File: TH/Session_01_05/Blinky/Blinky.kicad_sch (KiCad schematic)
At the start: 8 parts

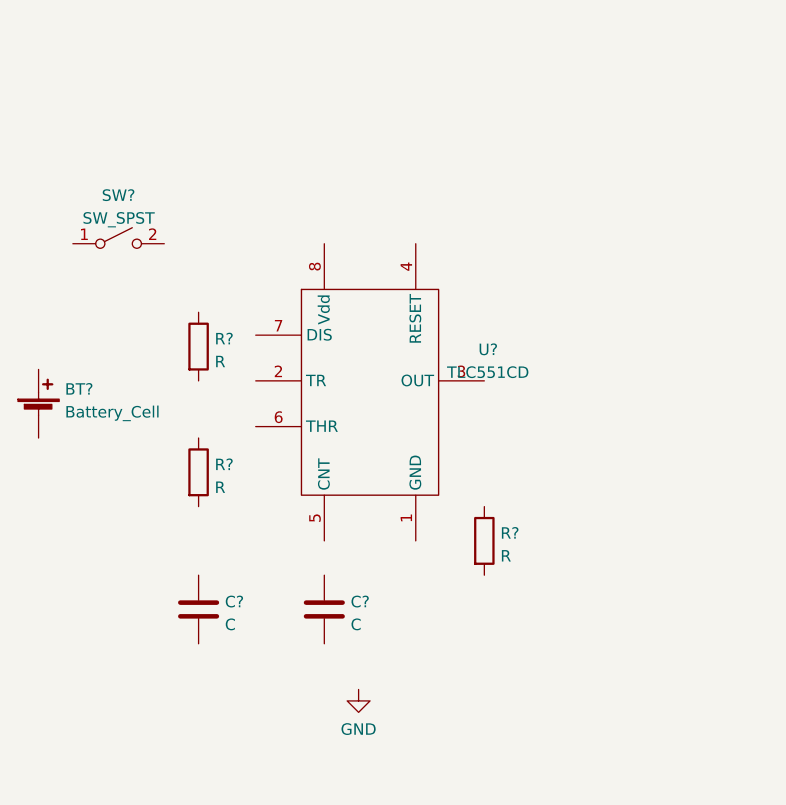
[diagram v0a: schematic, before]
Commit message: Revamps the through-hole project as transistor based
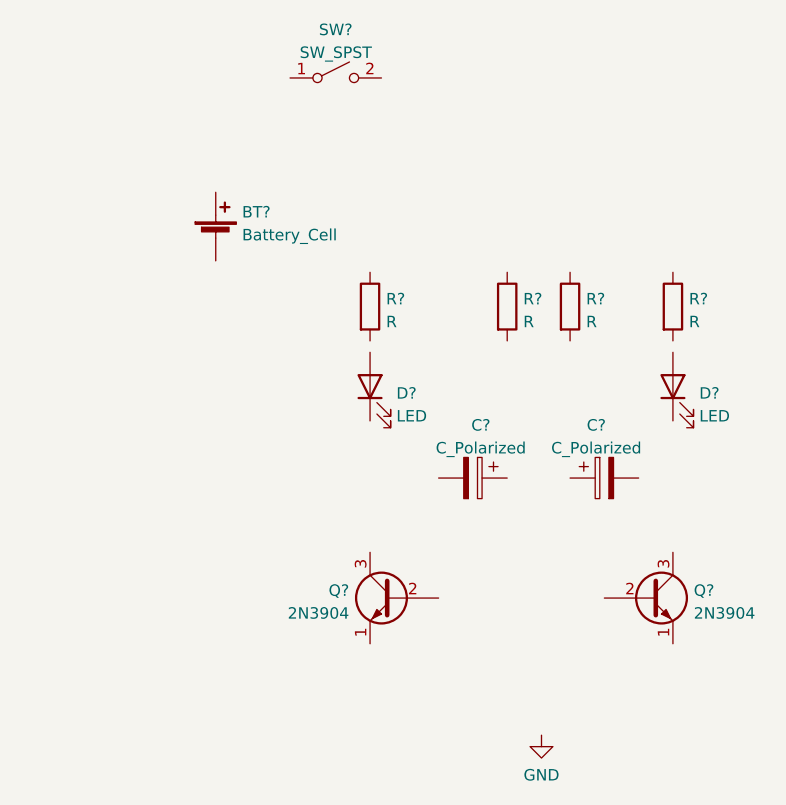
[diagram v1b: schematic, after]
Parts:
- removed BT?: Battery_Cell, symbol Device:Battery_Cell
- removed C? (x2): C, symbol Device:C
- removed R? (x3): R, symbol Device:R
- removed SW?: SW_SPST, symbol Switch:SW_SPST
- removed U?: TLC551CD‎, Package_SO:SOIC-8_3.9x4.9mm_P1.27mm, symbol Blinky:TLC551CD‎
- added BT?: Battery_Cell, symbol Device:Battery_Cell
- added C? (x2): C_Polarized, symbol Device:C_Polarized
- added D? (x2): LED, symbol Device:LED
- added Q? (x2): 2N3904, Package_TO_SOT_THT:TO-92_Inline, symbol Transistor_BJT:2N3904
- added R? (x4): R, symbol Device:R
- added SW?: SW_SPST, symbol Switch:SW_SPST
